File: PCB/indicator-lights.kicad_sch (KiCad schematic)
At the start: 8 parts, among them IC7 IS31FL3218-GRLS2

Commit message: re-annotate schematic
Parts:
- renumbered IC7 to IC9, R35 to R29
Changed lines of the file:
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@@
         )
         (path "/e89dcd22-1250-4a5b-b778-1c95a0dd623d/49c51f54-e113-47ff-b1ad-86c9ad73cafa"
-          (reference "C57") (unit 1)
+          (reference "C62") (unit 1)
         )
       )
@@
   (symbol (lib_id "power:+3V3") (at 153.67 73.66 0) (unit 1)
     (in_bom yes) (on_board yes) (dnp no) (fields_autoplaced)
-    (property "Reference" "#PWR079" (at 153.67 77.47 0)
+    (property "Reference" "#PWR082" (at 153.67 77.47 0)
       (effects (font (size 1.27 1.27)) hide)
     )
@@
       (project "OroLink"
         (path "/e89dcd22-1250-4a5b-b778-1c95a0dd623d/49c51f54-e113-47ff-b1ad-86c9ad73cafa"
-          (reference "#PWR079") (unit 1)
+          (reference "#PWR082") (unit 1)
         )
       )
@@
         )
         (path "/e89dcd22-1250-4a5b-b778-1c95a0dd623d/49c51f54-e113-47ff-b1ad-86c9ad73cafa"
-          (reference "C56") (unit 1)
+          (reference "C61") (unit 1)
         )
       )
@@
   (symbol (lib_id "power:GND") (at 87.63 113.03 0) (unit 1)
     (in_bom yes) (on_board yes) (dnp no) (fields_autoplaced)
-    (property "Reference" "#PWR078" (at 87.63 119.38 0)
+    (property "Reference" "#PWR081" (at 87.63 119.38 0)
       (effects (font (size 1.27 1.27)) hide)
     )
@@
       (project "OroLink"
         (path "/e89dcd22-1250-4a5b-b778-1c95a0dd623d/49c51f54-e113-47ff-b1ad-86c9ad73cafa"
-          (reference "#PWR078") (unit 1)
+          (reference "#PWR081") (unit 1)
         )
       )
@@
   (symbol (lib_id "power:+3V3") (at 87.63 91.44 0) (unit 1)
     (in_bom yes) (on_board yes) (dnp no) (fields_autoplaced)
-    (property "Reference" "#PWR077" (at 87.63 95.25 0)
+    (property "Reference" "#PWR080" (at 87.63 95.25 0)
       (effects (font (size 1.27 1.27)) hide)
     )
@@
       (project "OroLink"
         (path "/e89dcd22-1250-4a5b-b778-1c95a0dd623d/49c51f54-e113-47ff-b1ad-86c9ad73cafa"
-          (reference "#PWR077") (unit 1)
+          (reference "#PWR080") (unit 1)
         )
       )
@@
   (symbol (lib_id "SamacSys_Parts:IS31FL3218-GRLS2") (at 119.38 96.52 0) (unit 1)
     (in_bom yes) (on_board yes) (dnp no) (fields_autoplaced)
-    (property "Reference" "IC7" (at 135.89 91.0209 0)
+    (property "Reference" "IC9" (at 135.89 91.0209 0)
       (effects (font (size 1.27 1.27)))
     )
@@
       (project "OroLink"
         (path "/e89dcd22-1250-4a5b-b778-1c95a0dd623d/49c51f54-e113-47ff-b1ad-86c9ad73cafa"
-          (reference "IC7") (unit 1)
+          (reference "IC9") (unit 1)
         )
       )
@@
         )
         (path "/e89dcd22-1250-4a5b-b778-1c95a0dd623d/49c51f54-e113-47ff-b1ad-86c9ad73cafa"
-          (reference "R36") (unit 1)
+          (reference "R30") (unit 1)
         )
       )
@@
   (symbol (lib_id "power:+3V3") (at 171.45 73.66 0) (unit 1)
     (in_bom yes) (on_board yes) (dnp no) (fields_autoplaced)
-    (property "Reference" "#PWR080" (at 171.45 77.47 0)
+    (property "Reference" "#PWR083" (at 171.45 77.47 0)
       (effects (font (size 1.27 1.27)) hide)
     )
@@
       (project "OroLink"
         (path "/e89dcd22-1250-4a5b-b778-1c95a0dd623d/49c51f54-e113-47ff-b1ad-86c9ad73cafa"
-          (reference "#PWR080") (unit 1)
+          (reference "#PWR083") (unit 1)
         )
       )
@@
   (symbol (lib_id "SamacSys_Parts:CRGP0402F5K6") (at 88.9 109.22 0) (unit 1)
     (in_bom yes) (on_board yes) (dnp no)
-    (property "Reference" "R35" (at 95.25 106.68 0)
+    (property "Reference" "R29" (at 95.25 106.68 0)
       (effects (font (size 1.27 1.27)))
     )
@@
       (project "OroLink"
         (path "/e89dcd22-1250-4a5b-b778-1c95a0dd623d/49c51f54-e113-47ff-b1ad-86c9ad73cafa"
-          (reference "R35") (unit 1)
-        )
-      )
+          (reference "R29") (unit 1)
+        )
+      )

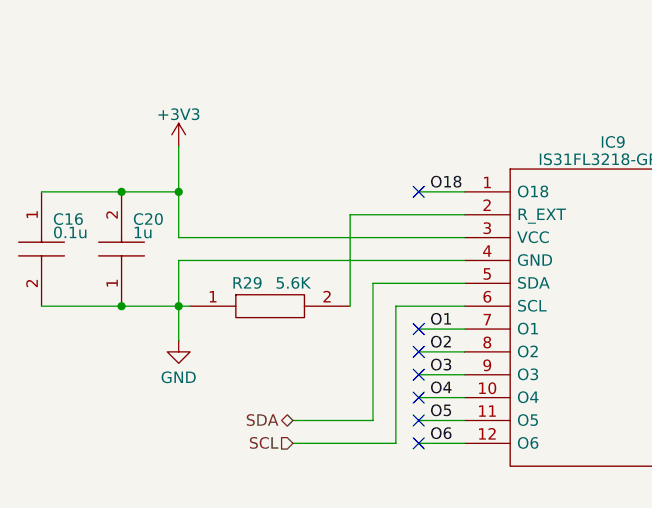
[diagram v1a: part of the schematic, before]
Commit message: add pullup/down resistors and fix oro 6p lines with boot1/0
closes #24
closes #21
closes #15
closes #12
closes #6
closes #3
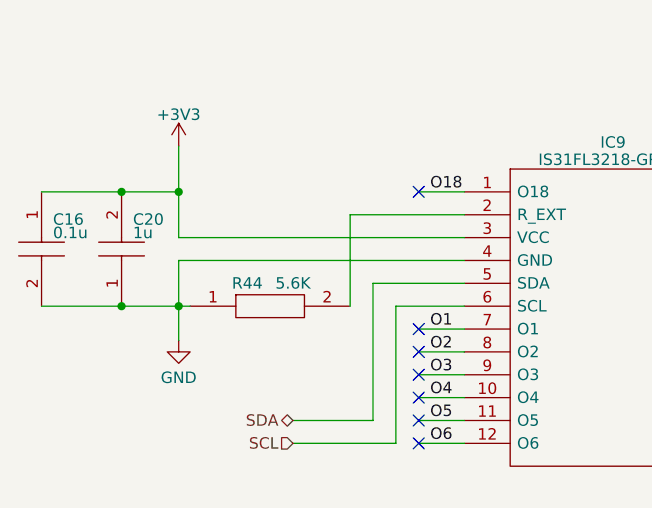
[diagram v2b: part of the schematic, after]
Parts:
- renumbered R29 to R44
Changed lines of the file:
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@@
   (symbol (lib_id "power:+3V3") (at 153.67 73.66 0) (unit 1)
     (in_bom yes) (on_board yes) (dnp no) (fields_autoplaced)
-    (property "Reference" "#PWR082" (at 153.67 77.47 0)
+    (property "Reference" "#PWR085" (at 153.67 77.47 0)
       (effects (font (size 1.27 1.27)) hide)
     )
@@
       (project "OroLink"
         (path "/e89dcd22-1250-4a5b-b778-1c95a0dd623d/49c51f54-e113-47ff-b1ad-86c9ad73cafa"
-          (reference "#PWR082") (unit 1)
+          (reference "#PWR085") (unit 1)
         )
       )
@@
   (symbol (lib_id "power:GND") (at 87.63 113.03 0) (unit 1)
     (in_bom yes) (on_board yes) (dnp no) (fields_autoplaced)
-    (property "Reference" "#PWR081" (at 87.63 119.38 0)
+    (property "Reference" "#PWR084" (at 87.63 119.38 0)
       (effects (font (size 1.27 1.27)) hide)
     )
@@
       (project "OroLink"
         (path "/e89dcd22-1250-4a5b-b778-1c95a0dd623d/49c51f54-e113-47ff-b1ad-86c9ad73cafa"
-          (reference "#PWR081") (unit 1)
+          (reference "#PWR084") (unit 1)
         )
       )
@@
   (symbol (lib_id "power:+3V3") (at 87.63 91.44 0) (unit 1)
     (in_bom yes) (on_board yes) (dnp no) (fields_autoplaced)
-    (property "Reference" "#PWR080" (at 87.63 95.25 0)
+    (property "Reference" "#PWR083" (at 87.63 95.25 0)
       (effects (font (size 1.27 1.27)) hide)
     )
@@
       (project "OroLink"
         (path "/e89dcd22-1250-4a5b-b778-1c95a0dd623d/49c51f54-e113-47ff-b1ad-86c9ad73cafa"
-          (reference "#PWR080") (unit 1)
+          (reference "#PWR083") (unit 1)
         )
       )
@@
         )
         (path "/e89dcd22-1250-4a5b-b778-1c95a0dd623d/49c51f54-e113-47ff-b1ad-86c9ad73cafa"
-          (reference "R30") (unit 1)
+          (reference "R45") (unit 1)
         )
       )
@@
   (symbol (lib_id "power:+3V3") (at 171.45 73.66 0) (unit 1)
     (in_bom yes) (on_board yes) (dnp no) (fields_autoplaced)
-    (property "Reference" "#PWR083" (at 171.45 77.47 0)
+    (property "Reference" "#PWR086" (at 171.45 77.47 0)
       (effects (font (size 1.27 1.27)) hide)
     )
@@
       (project "OroLink"
         (path "/e89dcd22-1250-4a5b-b778-1c95a0dd623d/49c51f54-e113-47ff-b1ad-86c9ad73cafa"
-          (reference "#PWR083") (unit 1)
+          (reference "#PWR086") (unit 1)
         )
       )
@@
   (symbol (lib_id "SamacSys_Parts:CRGP0402F5K6") (at 88.9 109.22 0) (unit 1)
     (in_bom yes) (on_board yes) (dnp no)
-    (property "Reference" "R29" (at 95.25 106.68 0)
+    (property "Reference" "R44" (at 95.25 106.68 0)
       (effects (font (size 1.27 1.27)))
     )
@@
       (project "OroLink"
         (path "/e89dcd22-1250-4a5b-b778-1c95a0dd623d/49c51f54-e113-47ff-b1ad-86c9ad73cafa"
-          (reference "R29") (unit 1)
-        )
-      )
+          (reference "R44") (unit 1)
+        )
+      )

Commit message: put pulldowns on unused OLED data lines and add a 510k to pin 13
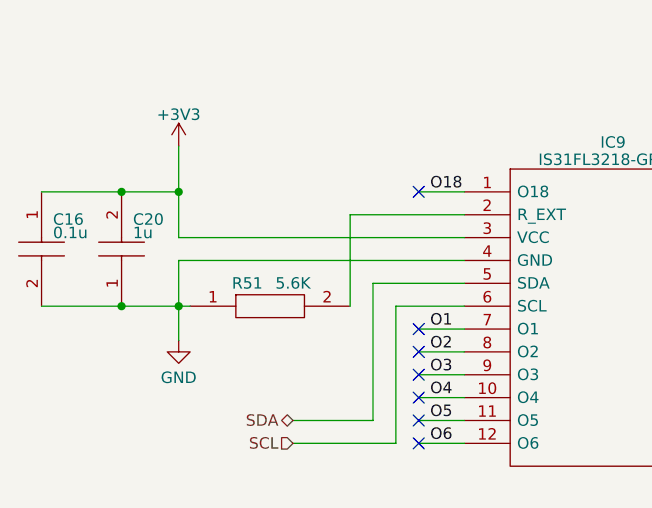
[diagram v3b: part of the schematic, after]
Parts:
- renumbered R44 to R51
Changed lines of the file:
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@@
         )
         (path "/e89dcd22-1250-4a5b-b778-1c95a0dd623d/49c51f54-e113-47ff-b1ad-86c9ad73cafa"
-          (reference "R45") (unit 1)
+          (reference "R52") (unit 1)
         )
       )
@@
   (symbol (lib_id "SamacSys_Parts:CRGP0402F5K6") (at 88.9 109.22 0) (unit 1)
     (in_bom yes) (on_board yes) (dnp no)
-    (property "Reference" "R44" (at 95.25 106.68 0)
+    (property "Reference" "R51" (at 95.25 106.68 0)
       (effects (font (size 1.27 1.27)))
     )
@@
       (project "OroLink"
         (path "/e89dcd22-1250-4a5b-b778-1c95a0dd623d/49c51f54-e113-47ff-b1ad-86c9ad73cafa"
-          (reference "R44") (unit 1)
+          (reference "R51") (unit 1)
         )
       )

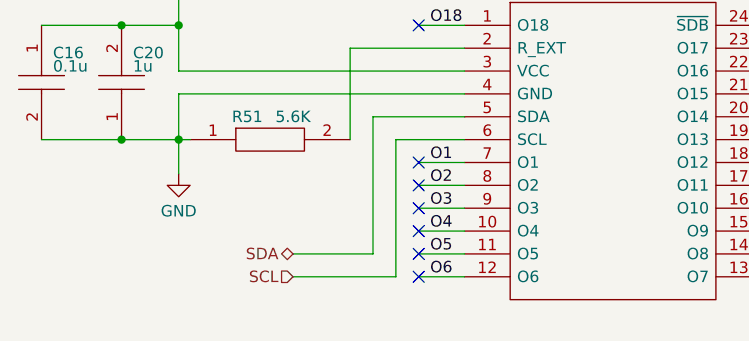
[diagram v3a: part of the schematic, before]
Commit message: add debug pins to signal lines (closes #16)
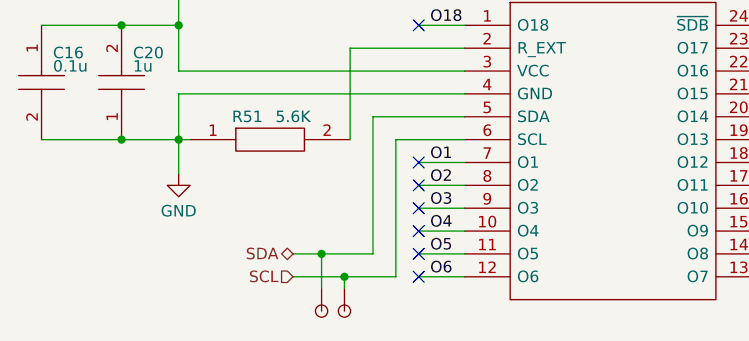
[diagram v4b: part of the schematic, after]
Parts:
- added DBG5 (x2): ~, Oro Footprints:DebugPin, symbol Oro:DebugPin
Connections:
- net SCL: now also DBG5.1
- net SDA: now also DBG5.1
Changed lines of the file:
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@@
   (junction (at 87.63 96.52) (diameter 0) (color 0 0 0 0)
   )
+  (junction (at 103.505 121.92) (diameter 0) (color 0 0 0 0)
+  )
   (junction (at 81.28 109.22) (diameter 0) (color 0 0 0 0)
   )
   (junction (at 171.45 91.44) (diameter 0) (color 0 0 0 0)
+  )
+  (junction (at 106.045 124.46) (diameter 0) (color 0 0 0 0)
   )
   (junction (at 87.63 109.22) (diameter 0) (color 0 0 0 0)
@@
     (stroke (width 0) (type default))
   )
-  (wire (pts (xy 100.33 121.92) (xy 109.22 121.92))
+  (wire (pts (xy 100.33 121.92) (xy 103.505 121.92))
     (stroke (width 0) (type default))
   )
@@
     (stroke (width 0) (type default))
   )
+  (wire (pts (xy 103.505 121.92) (xy 109.22 121.92))
+    (stroke (width 0) (type default))
+  )
   (wire (pts (xy 208.28 124.46) (xy 204.47 124.46))
     (stroke (width 0) (type default))
@@
     (stroke (width 0) (type default))
   )
+  (wire (pts (xy 103.505 121.92) (xy 103.505 125.73))
+    (stroke (width 0) (type default))
+  )
   (wire (pts (xy 156.21 119.38) (xy 152.4 119.38))
     (stroke (width 0) (type default))
@@
     (stroke (width 0) (type default))
   )
+  (wire (pts (xy 106.045 124.46) (xy 111.76 124.46))
+    (stroke (width 0) (type default))
+  )
   (wire (pts (xy 114.3 111.76) (xy 119.38 111.76))
     (stroke (width 0) (type default))
@@
     (stroke (width 0) (type default))
   )
+  (wire (pts (xy 106.045 124.46) (xy 106.045 125.73))
+    (stroke (width 0) (type default))
+  )
   (wire (pts (xy 72.39 109.22) (xy 81.28 109.22))
     (stroke (width 0) (type default))
@@
     (stroke (width 0) (type default))
   )
-  (wire (pts (xy 100.33 124.46) (xy 111.76 124.46))
+  (wire (pts (xy 100.33 124.46) (xy 106.045 124.46))
     (stroke (width 0) (type default))
   )
@@
     )
   )
+  (symbol (lib_id "Oro:DebugPin") (at 103.505 125.73 270) (unit 1)
+    (in_bom no) (on_board yes) (dnp no)
+    (property "Reference" "DBG5" (at 103.505 131.445 0)
+      (effects (font (size 1.27 1.27)) hide)
+    )
+    (property "Value" "~" (at 103.505 125.73 0)
+      (effects (font (size 1.27 1.27)) hide)
+    )
+    (property "Footprint" "Oro Footprints:DebugPin" (at 106.045 127 0)
+      (effects (font (size 1.27 1.27)) hide)
+    )
+    (property "Datasheet" "" (at 103.505 125.73 0)
+      (effects (font (size 1.27 1.27)) hide)
+    )
+    (property "Sim.Enable" "0" (at 106.045 139.7 0)
+      (effects (font (size 1.27 1.27)) hide)
+    )
+    (pin "1")
+    (instances
+      (project "OroLink"
+        (path "/e89dcd22-1250-4a5b-b778-1c95a0dd623d/f955395e-bf1a-4ef3-9cfe-ec9d49f66988"
+          (reference "DBG5") (unit 1)
+        )
+        (path "/e89dcd22-1250-4a5b-b778-1c95a0dd623d/1b3eede1-74b0-4c0b-b4f1-7ec1bfc1f54f"
+          (reference "DBG16") (unit 1)
+        )
+        (path "/e89dcd22-1250-4a5b-b778-1c95a0dd623d/52771c01-2e58-4900-abe5-411f688d020f"
+          (reference "DBG25") (unit 1)
+        )
+        (path "/e89dcd22-1250-4a5b-b778-1c95a0dd623d/7cebe953-3148-4b67-a6c9-1f2594261687"
+          (reference "DBG26") (unit 1)
+        )
+        (path "/e89dcd22-1250-4a5b-b778-1c95a0dd623d/49c51f54-e113-47ff-b1ad-86c9ad73cafa"
+          (reference "DBG31") (unit 1)
+        )
+      )
+    )
+  )
   (symbol (lib_id "SamacSys_Parts:RC2010JK-0710KL") (at 153.67 76.2 270) (unit 1)
     (in_bom yes) (on_board yes) (dnp no)
@@
         )
       )
+    )
+  )
+  (symbol (lib_id "Oro:DebugPin") (at 106.045 125.73 270) (unit 1)
+    (in_bom no) (on_board yes) (dnp no)
+    (property "Reference" "DBG5" (at 106.045 131.445 0)
+      (effects (font (size 1.27 1.27)) hide)
+    )
+    (property "Value" "~" (at 106.045 125.73 0)
+      (effects (font (size 1.27 1.27)) hide)
+    )
+    (property "Footprint" "Oro Footprints:DebugPin" (at 108.585 127 0)
+      (effects (font (size 1.27 1.27)) hide)
+    )
+    (property "Datasheet" "" (at 106.045 125.73 0)
+      (effects (font (size 1.27 1.27)) hide)
+    )
+    (property "Sim.Enable" "0" (at 108.585 139.7 0)
+      (effects (font (size 1.27 1.27)) hide)
+    )
+    (pin "1")
+    (instances
+      (project "OroLink"
+        (path "/e89dcd22-1250-4a5b-b778-1c95a0dd623d/f955395e-bf1a-4ef3-9cfe-ec9d49f66988"
+          (reference "DBG5") (unit 1)
+        )
+        (path "/e89dcd22-1250-4a5b-b778-1c95a0dd623d/1b3eede1-74b0-4c0b-b4f1-7ec1bfc1f54f"
+          (reference "DBG16") (unit 1)
+        )
+        (path "/e89dcd22-1250-4a5b-b778-1c95a0dd623d/52771c01-2e58-4900-abe5-411f688d020f"
+          (reference "DBG25") (unit 1)
+        )
+        (path "/e89dcd22-1250-4a5b-b778-1c95a0dd623d/7cebe953-3148-4b67-a6c9-1f2594261687"
+          (reference "DBG26") (unit 1)
+        )
+        (path "/e89dcd22-1250-4a5b-b778-1c95a0dd623d/49c51f54-e113-47ff-b1ad-86c9ad73cafa"
+          (reference "DBG32") (unit 1)
+        )
+      )

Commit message: switch 10k and 4.7k resistors to smaller packages (closes #32)
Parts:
- R10: footprint SamacSys_Parts:RESC5025X65N -> RESC5025X65N
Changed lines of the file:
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@@
       (effects (font (size 1.27 1.27)) (justify right))
     )
-    (property "Footprint" "SamacSys_Parts:RESC5025X65N" (at 154.94 90.17 0)
+    (property "Footprint" "RESC5025X65N" (at 154.94 90.17 0)
       (effects (font (size 1.27 1.27)) (justify left) hide)
     )

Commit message: actually reduce 10k package size (ref #32)
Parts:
- R10: footprint RESC5025X65N -> RESC1005X40N; symbol SamacSys_Parts:RC2010JK-0710KL -> SamacSys_Parts:RK73H1ETTP1002F; Arrow Part Number RC2010JK-0710KL -> RK73H1ETTP1002F; Arrow Price/Stock https://www.arrow.com/en/products/rc2010jk-0710kl/yageo -> https://www.arrow.com/en/products/rk73h1ettp1002f/koa-speer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; Height 0.65 -> 0.4; Manufacturer_Name KEMET -> KOA Speer; Manufacturer_Part_Number RC2010JK-0710KL -> RK73H1ETTP1002F; Mouser Part Number 603-RC2010JK-0710KL -> 660-RK73H1ETTP1002F; Mouser Price/Stock https://www.mouser.co.uk/ProductDetail/YAGEO/RC2010JK-0710K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 -> https://www.mouser.co.uk/ProductDetail/KOA-Speer/RK73H1ETTP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
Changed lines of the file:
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@@
     )
   )
-  (symbol (lib_id "SamacSys_Parts:RC2010JK-0710KL") (at 153.67 76.2 270) (unit 1)
+  (symbol (lib_id "SamacSys_Parts:RK73H1ETTP1002F") (at 153.67 76.2 270) (unit 1)
     (in_bom yes) (on_board yes) (dnp no)
     (property "Reference" "R10" (at 160.02 83.82 90)
@@
       (effects (font (size 1.27 1.27)) (justify right))
     )
-    (property "Footprint" "RESC5025X65N" (at 154.94 90.17 0)
+    (property "Footprint" "RESC1005X40N" (at 154.94 90.17 0)
       (effects (font (size 1.27 1.27)) (justify left) hide)
     )
-    (property "Datasheet" "https://www.arrow.com/en/products/rc2010jk-0710kl/yageo" (at 152.4 90.17 0)
+    (property "Datasheet" "http://www.koaspeer.com/catimages/Products/RK73-RT/RK73-RT.pdf" (at 152.4 90.17 0)
       (effects (font (size 1.27 1.27)) (justify left) hide)
     )
-    (property "Description" "Res Thick Film 2010 10K Ohm 5% 0.75W(3/4W) +/-100ppm/C Pad SMD T/R" (at 149.86 90.17 0)
+    (property "Description" "Resistor,ThickFilm1005,0.063W,10kohm" (at 149.86 90.17 0)
       (effects (font (size 1.27 1.27)) (justify left) hide)
     )
-    (property "Height" "0.65" (at 147.32 90.17 0)
+    (property "Height" "0.4" (at 147.32 90.17 0)
       (effects (font (size 1.27 1.27)) (justify left) hide)
     )
-    (property "Manufacturer_Name" "KEMET" (at 144.78 90.17 0)
+    (property "Manufacturer_Name" "KOA Speer" (at 144.78 90.17 0)
       (effects (font (size 1.27 1.27)) (justify left) hide)
     )
-    (property "Manufacturer_Part_Number" "RC2010JK-0710KL" (at 142.24 90.17 0)
+    (property "Manufacturer_Part_Number" "RK73H1ETTP1002F" (at 142.24 90.17 0)
       (effects (font (size 1.27 1.27)) (justify left) hide)
     )
-    (property "Mouser Part Number" "603-RC2010JK-0710KL" (at 139.7 90.17 0)
+    (property "Mouser Part Number" "660-RK73H1ETTP1002F" (at 139.7 90.17 0)
       (effects (font (size 1.27 1.27)) (justify left) hide)
     )
-    (property "Mouser Price/Stock" "https://www.mouser.co.uk/ProductDetail/YAGEO/RC2010JK-0710KL?qs=sNpmnPgvziOLj5uuquGIow%3D%3D" (at 137.16 90.17 0)
+    (property "Mouser Price/Stock" "https://www.mouser.co.uk/ProductDetail/KOA-Speer/RK73H1ETTP1002F?qs=uLfVlVfCHH2OZ4JTybrBPQ%3D%3D" (at 137.16 90.17 0)
       (effects (font (size 1.27 1.27)) (justify left) hide)
     )
-    (property "Arrow Part Number" "RC2010JK-0710KL" (at 134.62 90.17 0)
+    (property "Arrow Part Number" "RK73H1ETTP1002F" (at 134.62 90.17 0)
       (effects (font (size 1.27 1.27)) (justify left) hide)
     )
-    (property "Arrow Price/Stock" "https://www.arrow.com/en/products/rc2010jk-0710kl/yageo" (at 132.08 90.17 0)
+    (property "Arrow Price/Stock" "https://www.arrow.com/en/products/rk73h1ettp1002f/koa-speer-electronics?region=nac" (at 132.08 90.17 0)
       (effects (font (size 1.27 1.27)) (justify left) hide)
     )

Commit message: re-annotate schematic
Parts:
- renumbered R51 to R53
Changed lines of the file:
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@@
         )
         (path "/e89dcd22-1250-4a5b-b778-1c95a0dd623d/49c51f54-e113-47ff-b1ad-86c9ad73cafa"
-          (reference "R52") (unit 1)
+          (reference "R54") (unit 1)
         )
       )
@@
   (symbol (lib_id "SamacSys_Parts:CRGP0402F5K6") (at 88.9 109.22 0) (unit 1)
     (in_bom yes) (on_board yes) (dnp no)
-    (property "Reference" "R51" (at 95.25 106.68 0)
+    (property "Reference" "R53" (at 95.25 106.68 0)
       (effects (font (size 1.27 1.27)))
     )
@@
       (project "OroLink"
         (path "/e89dcd22-1250-4a5b-b778-1c95a0dd623d/49c51f54-e113-47ff-b1ad-86c9ad73cafa"
-          (reference "R51") (unit 1)
+          (reference "R53") (unit 1)
         )
       )
